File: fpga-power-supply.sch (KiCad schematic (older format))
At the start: 88 parts, among them U14 XC7A100T-FGG484

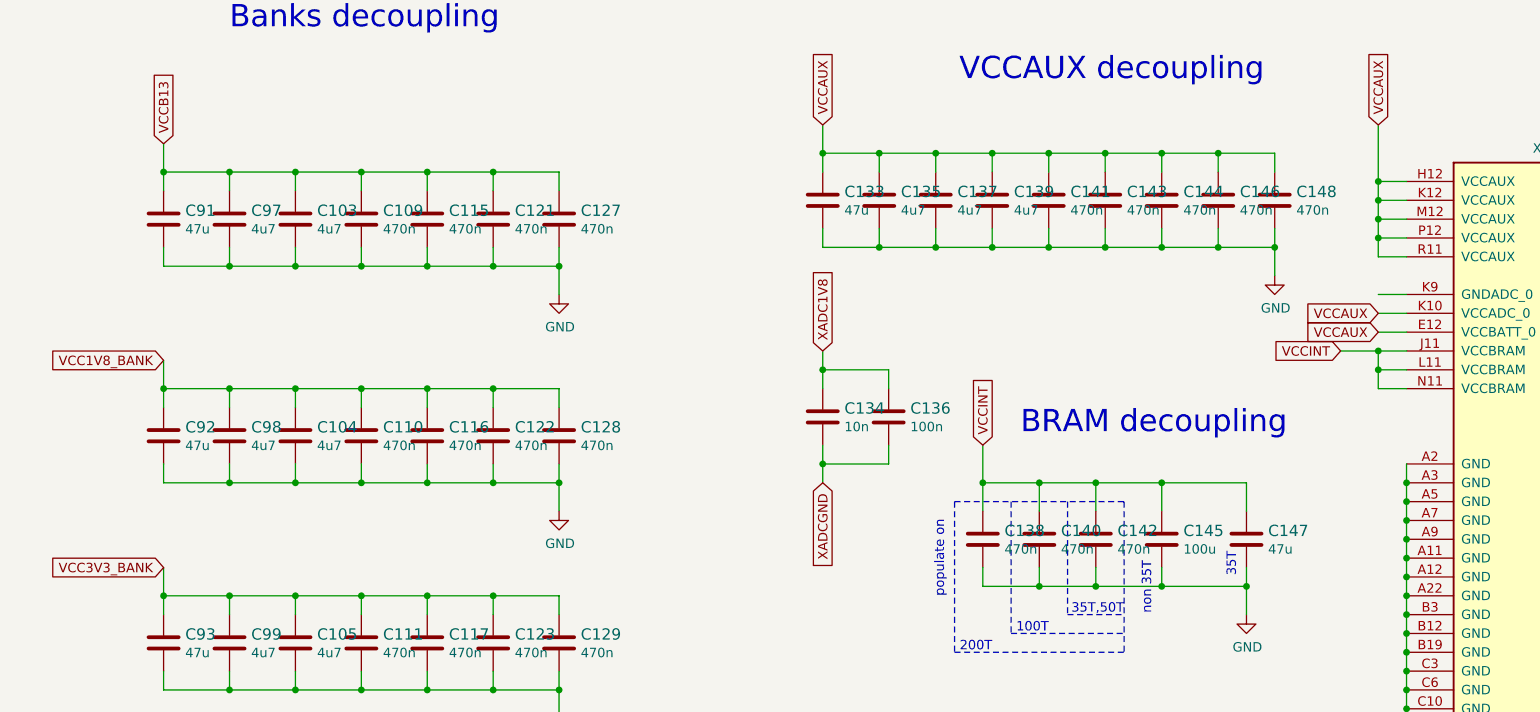
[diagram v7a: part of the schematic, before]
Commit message: FPGA related fixes, removed floating tags from Interfaces
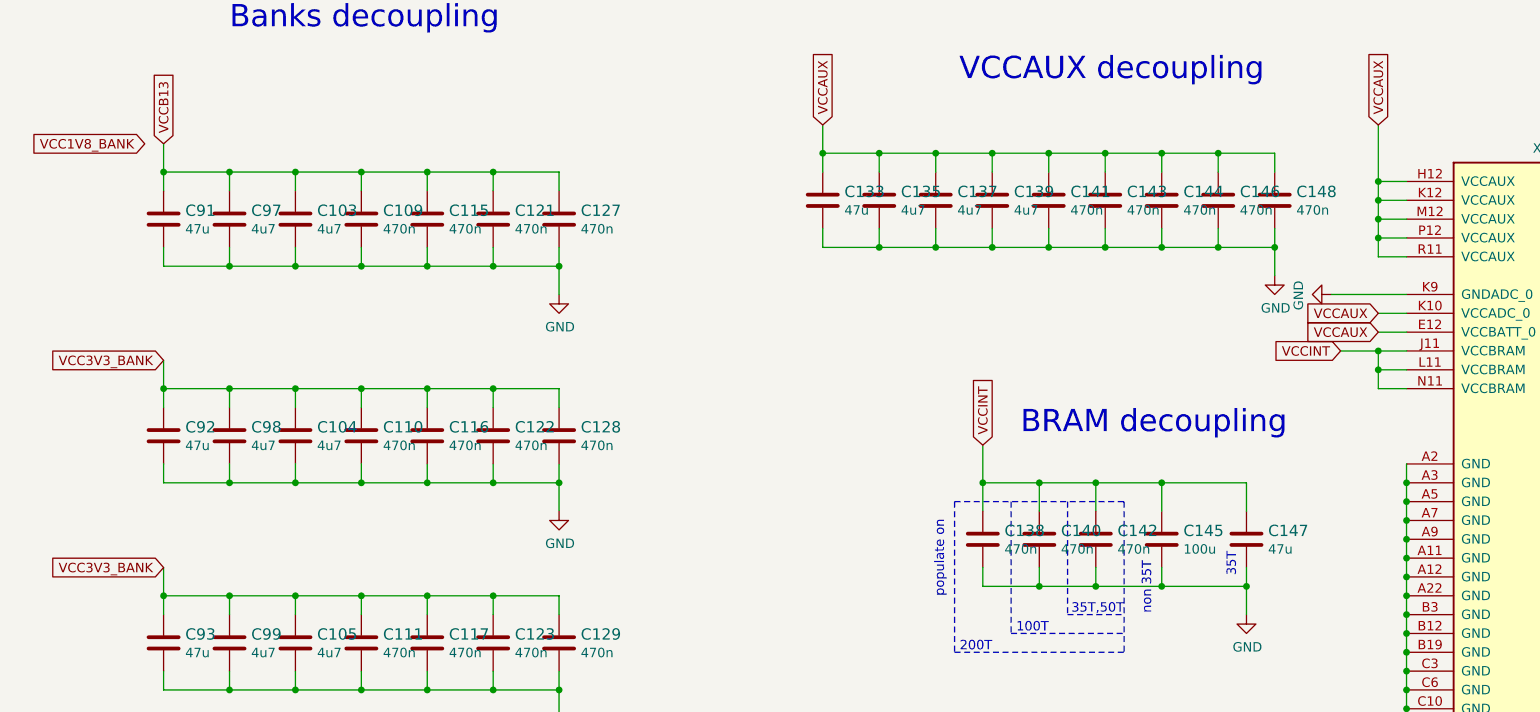
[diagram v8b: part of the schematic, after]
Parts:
- removed C134: C_10n_0402, artix-dc-scm-footprints:0402-cap, symbol artix-dc-scm:C_10n_0402
- removed C136: C_100n_0402, artix-dc-scm-footprints:0402-cap, symbol artix-dc-scm:C_100n_0402
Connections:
- net GND: now also U14.K9 (GNDADC_0)
- net VCC1V8_BANK: no longer C104.1, C110.1, C116.1, C122.1, C128.1, C92.1, C98.1
- net VCC3V3_BANK: now also C104.1, C110.1, C116.1, C122.1, C128.1, C92.1, C98.1
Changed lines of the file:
@@
 Wire Wire Line
 	7750 3600 7600 3600
-Text GLabel 4650 3800 1    50   Input ~ 0
-XADC1V8
-$Comp
-L artix-dc-scm:C_10n_0402 C?
-U 1 1 6188C046
-P 4650 4150
-AR Path="/626D078D/6188C046" Ref="C?"  Part="1"
-AR Path="/605FD480/6188C046" Ref="C?"  Part="1"
-AR Path="/60633613/6188C046" Ref="C?"  Part="1"
-AR Path="/5FD86C51/6188C046" Ref="C134"  Part="1"
-F 0 "C134" H 4765 4195 60  0000 L CNN
-F 1 "C_10n_0402" H 4650 4000 60  0001 C CNN
-F 2 "artix-dc-scm-footprints:0402-cap" H 4850 4350 60  0001 L CNN
-F 3 "" H 4650 4150 50  0001 C CNN
-F 4 "AVX" H 4850 4550 60  0001 L CNN "Manufacturer"
-F 5 "04025G103ZAT2A" H 4850 4450 60  0001 L CNN "MPN"
-F 6 "10n" H 4765 4097 50  0000 L CNN "Val"
-	1    4650 4150
-	1    0    0    -1
-$EndComp
-$Comp
-L artix-dc-scm:C_100n_0402 C?
-U 1 1 6188CD94
-P 5000 4150
-AR Path="/626D078D/6188CD94" Ref="C?"  Part="1"
-AR Path="/605FD480/6188CD94" Ref="C?"  Part="1"
-AR Path="/60633613/6188CD94" Ref="C?"  Part="1"
-AR Path="/5FD86C51/6188CD94" Ref="C136"  Part="1"
-F 0 "C136" H 5115 4195 60  0000 L CNN
-F 1 "C_100n_0402" H 5000 4000 60  0001 C CNN
-F 2 "artix-dc-scm-footprints:0402-cap" H 5200 4350 60  0001 L CNN
-F 3 "" H 5000 4150 50  0001 C CNN
-F 4 "Walsin" H 5200 4550 60  0001 L CNN "Manufacturer"
-F 5 "0402X104K6R3CT" H 5200 4450 60  0001 L CNN "MPN"
-F 6 "100n" H 5115 4097 50  0000 L CNN "Val"
-	1    5000 4150
-	1    0    0    -1
-$EndComp
-Wire Wire Line
-	5000 4000 5000 3900
-Wire Wire Line
-	5000 3900 4650 3900
-Wire Wire Line
-	4650 3900 4650 3800
-Wire Wire Line
-	4650 4000 4650 3900
-Connection ~ 4650 3900
-Wire Wire Line
-	5000 4300 5000 4400
-Wire Wire Line
-	5000 4400 4650 4400
-Wire Wire Line
-	4650 4400 4650 4300
-Wire Wire Line
-	4650 4400 4650 4500
-Connection ~ 4650 4400
-Wire Wire Line
-	7750 3500 7600 3500
-Text GLabel 4650 4500 3    50   Input ~ 0
-XADCGND
 $Comp
 L artix-dc-scm:C_47u_1210 C?
@@
 Text GLabel 11500 3900 1    50   Input ~ 0
 VCCINT
-Text GLabel 1150 3850 0    50   Input ~ 0
+Text GLabel 1050 2700 0    50   Input ~ 0
 VCC1V8_BANK
 Text GLabel 1150 4950 0    50   Input ~ 0
@@
 	1    0    0    -1
 $EndComp
+$Comp
+L artix-dc-scm:GND #PWR?
+U 1 1 61075D45
+P 7350 3500
+AR Path="/626D078D/61075D45" Ref="#PWR?"  Part="1"
+AR Path="/605FD480/61075D45" Ref="#PWR?"  Part="1"
+AR Path="/60633613/61075D45" Ref="#PWR?"  Part="1"
+AR Path="/5FD86C51/61075D45" Ref="#PWR?"  Part="1"
+F 0 "#PWR?" H 7350 3250 50  0001 C CNN
+F 1 "GND" H 7355 3327 50  0000 C CNN
+F 2 "" H 7350 3500 50  0001 C CNN
+F 3 "" H 7350 3500 50  0001 C CNN
+	1    7350 3500
+	0    1    1    0
+$EndComp
+Wire Wire Line
+	7350 3500 7750 3500
+Text GLabel 1150 3850 0    50   Input ~ 0
+VCC3V3_BANK
 $EndSCHEMATC
